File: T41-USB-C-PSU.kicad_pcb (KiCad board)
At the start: 4 copper layers, 50 x 18 mm, 64 parts, among them J1 USB_C_Receptacle_USB2.0, Q1 AP90P03Q, Q2 AP90P03Q, Q3 NTTFS4C25NTWG, U1 LM73606, U2 CYPD3177, U3 LM5069

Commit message: Hide silkscreen designators
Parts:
- added REF**: LED_0603_1608Metric, LED_SMD:LED_0603_1608Metric, F.Cu at (105.4, 102.5)
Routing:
- net GND: vias 66 -> 64

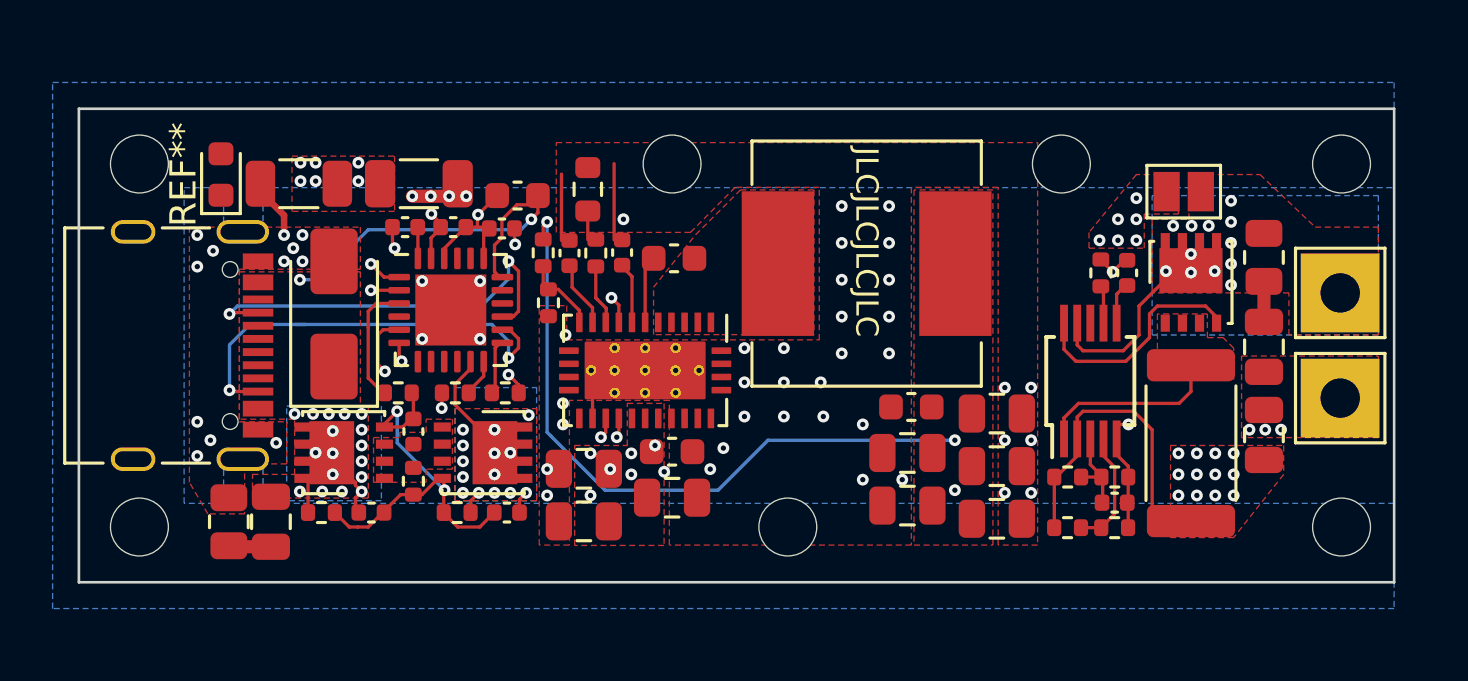
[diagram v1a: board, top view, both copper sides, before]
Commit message: Add tooling holes
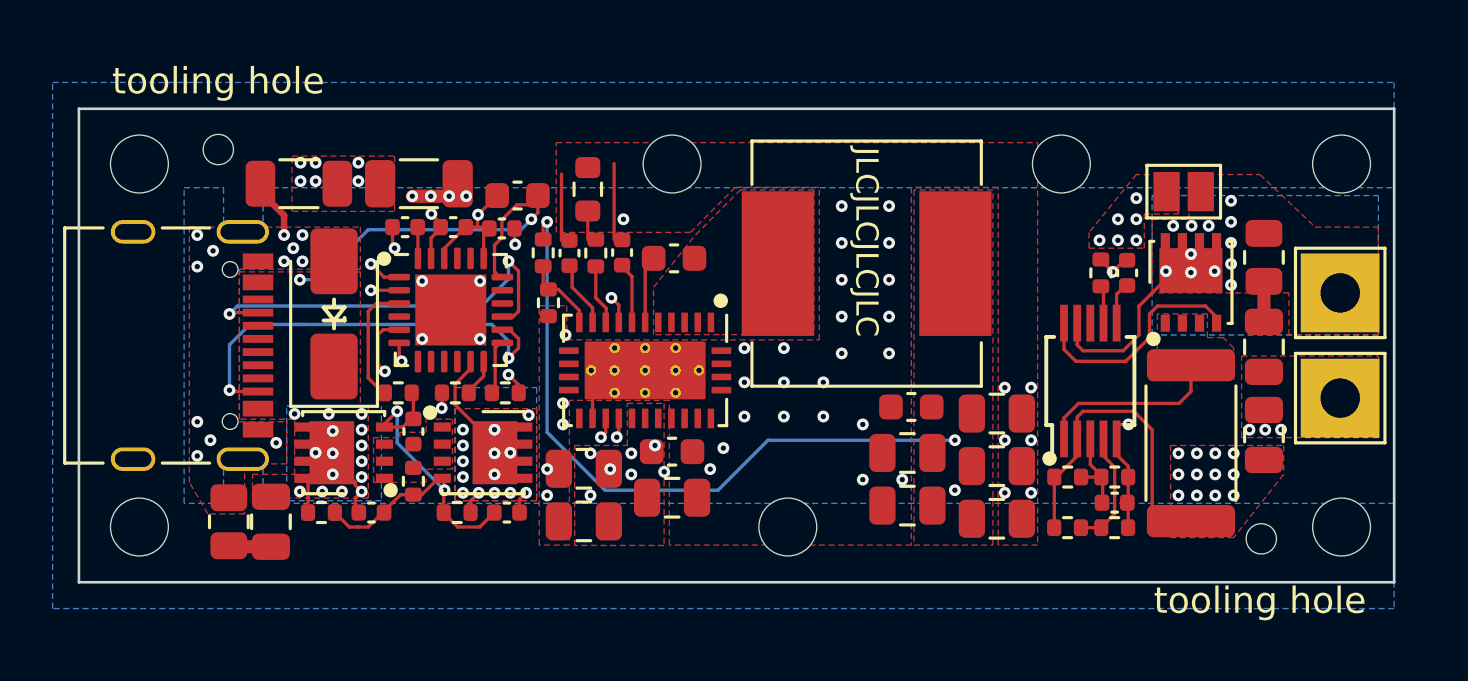
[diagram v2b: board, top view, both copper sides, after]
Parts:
- removed REF**: LED_0603_1608Metric, LED_SMD:LED_0603_1608Metric
- added H1: ToolingHole, ToolingHole:ToolingHole_JLCSMT, F.Cu at (144.9, 116.3)
- added H2: ToolingHole, ToolingHole:ToolingHole_JLCSMT, F.Cu at (105.3, 101.5)
- H3, H4, H5, H6, H7, H8, H9: renamed from REF**; value MountingHole_2.2mm_M2 -> MountingHole
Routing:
- net Net-(D1-A1): vias 19 -> 17

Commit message: Add status LEDs
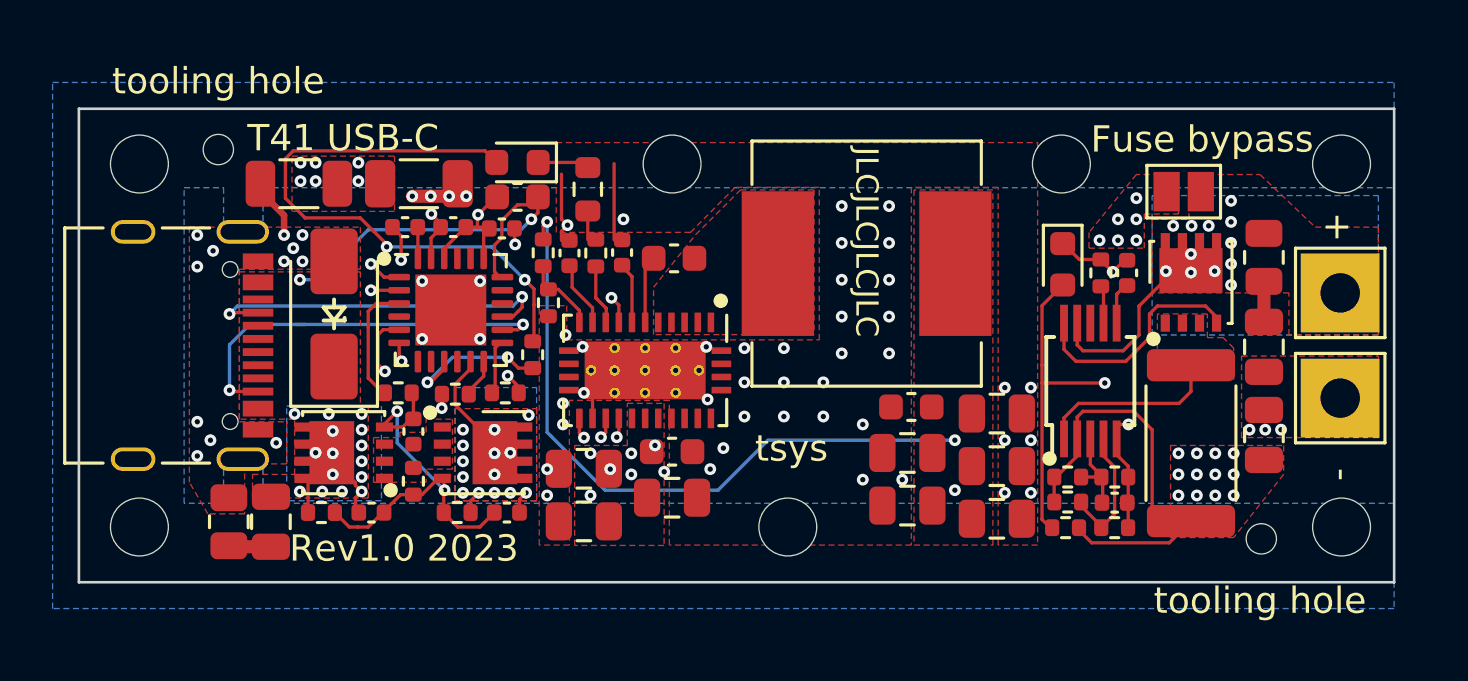
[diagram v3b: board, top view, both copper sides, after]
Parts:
- added D2: RED, LED_SMD:LED_0603_1608Metric, F.Cu at (116.7, 102.0)
- added D3: GRN, LED_SMD:LED_0603_1608Metric, F.Cu at (137.4, 105.9)
- added R19: 1k, Resistor_SMD:R_0402_1005Metric, F.Cu at (117.2, 109.3)
- added R20: 33k, Resistor_SMD:R_0402_1005Metric, F.Cu at (137.5, 115.9)
- moved R15 0.98 mm to (137.6, 115.0)
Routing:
- net /Buck converter/PGOOD: track 0.00 -> 42.3 mm, vias 0 -> 2
- net Net-(D2-A): track 0.00 -> 22.7 mm, vias 0 -> 2
- net /USB input/FAULT: track 0.00 -> 5.69 mm, vias 0 -> 2
- net GND: track 24.3 -> 28.4 mm, vias 64 -> 69
- net /Buck converter/VOUT: track 54.3 -> 58.1 mm
- net Net-(J1-CC1): track 15.7 -> 13.8 mm
- net Net-(J1-CC2): track 16.7 -> 15.8 mm
- net Net-(U3-OVLO): track 4.58 -> 5.09 mm
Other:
- board text added: "+"
- board text added: "-"
- board text added: "Fuse bypass"
- board text added: "Rev1.0 2023"
- board text added: "T41 USB-C"
- board text added: "tsys"

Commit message: Improve VOUT plane connectivity
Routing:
- net /Buck converter/VOUT: track 58.1 -> 58.3 mm, vias 22 -> 30
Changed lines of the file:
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@@
   (segment (start 117.65 104.966) (end 117.65 104.45) (width 0.127) (layer "F.Cu") (net 10))
   (via (at 143.2 113.1) (size 0.45) (drill 0.2) (layers "F.Cu" "B.Cu") (free) (net 10))
+  (via (at 133.9 112.6) (size 0.45) (drill 0.2) (layers "F.Cu" "B.Cu") (free) (net 10))
+  (via (at 132.075 114.1) (size 0.45) (drill 0.2) (layers "F.Cu" "B.Cu") (free) (net 10))
   (via (at 140.2 103.4) (size 0.45) (drill 0.2) (layers "F.Cu" "B.Cu") (free) (net 10))
   (via (at 133.3 112.6) (size 0.45) (drill 0.2) (layers "F.Cu" "B.Cu") (net 10))
@@
   (via (at 143.9 113.9) (size 0.45) (drill 0.2) (layers "F.Cu" "B.Cu") (free) (net 10))
   (via (at 143.2 114.7) (size 0.45) (drill 0.2) (layers "F.Cu" "B.Cu") (free) (net 10))
+  (via (at 134.5 112.6) (size 0.45) (drill 0.2) (layers "F.Cu" "B.Cu") (free) (net 10))
   (via (at 142.5 113.1) (size 0.45) (drill 0.2) (layers "F.Cu" "B.Cu") (free) (net 10))
   (via (at 138.8 105) (size 0.45) (drill 0.2) (layers "F.Cu" "B.Cu") (free) (net 10))
   (via (at 120.246 107.186) (size 0.45) (drill 0.2) (layers "F.Cu" "B.Cu") (net 10))
+  (via (at 133.2 113.25) (size 0.45) (drill 0.2) (layers "F.Cu" "B.Cu") (free) (net 10))
   (via (at 133.3 114.5) (size 0.45) (drill 0.2) (layers "F.Cu" "B.Cu") (free) (net 10))
   (via (at 141.8 113.9) (size 0.45) (drill 0.2) (layers "F.Cu" "B.Cu") (free) (net 10))
+  (via (at 132.65 114.1) (size 0.45) (drill 0.2) (layers "F.Cu" "B.Cu") (net 10))
   (via (at 142.5 114.7) (size 0.45) (drill 0.2) (layers "F.Cu" "B.Cu") (free) (net 10))
   (via (at 143.9 113.1) (size 0.45) (drill 0.2) (layers "F.Cu" "B.Cu") (free) (net 10))
@@
   (via (at 117.8 104.3) (size 0.45) (drill 0.2) (layers "F.Cu" "B.Cu") (net 10))
   (via (at 142.5 113.9) (size 0.45) (drill 0.2) (layers "F.Cu" "B.Cu") (free) (net 10))
+  (via (at 133.9 114.55) (size 0.45) (drill 0.2) (layers "F.Cu" "B.Cu") (free) (net 10))
   (via (at 140.2 105) (size 0.45) (drill 0.2) (layers "F.Cu" "B.Cu") (free) (net 10))
+  (via (at 133.2 113.9) (size 0.45) (drill 0.2) (layers "F.Cu" "B.Cu") (free) (net 10))
   (via (at 143.9 114.7) (size 0.45) (drill 0.2) (layers "F.Cu" "B.Cu") (free) (net 10))
+  (via (at 134.5 114.55) (size 0.45) (drill 0.2) (layers "F.Cu" "B.Cu") (free) (net 10))
   (via (at 141.8 113.1) (size 0.45) (drill 0.2) (layers "F.Cu" "B.Cu") (free) (net 10))
-  (segment (start 125.986 107.186) (end 133.3 114.5) (width 0.127) (layer "In2.Cu") (net 10))
+  (segment (start 132.65 114.1) (end 132.9 114.1) (width 0.127) (layer "In2.Cu") (net 10))
+  (segment (start 125.986 107.186) (end 132.65 113.85) (width 0.127) (layer "In2.Cu") (net 10))
   (segment (start 120.246 107.186) (end 125.986 107.186) (width 0.127) (layer "In2.Cu") (net 10))
+  (segment (start 132.65 113.85) (end 132.65 114.1) (width 0.127) (layer "In2.Cu") (net 10))
+  (segment (start 132.9 114.1) (end 133.3 114.5) (width 0.127) (layer "In2.Cu") (net 10))
   (segment (start 117.8 112.3) (end 117.95 112.45) (width 0.127) (layer "B.Cu") (net 10))
   (segment (start 120 114.5) (end 124.3 114.5) (width 0.127) (layer "B.Cu") (net 10))
@@
     (polygon
       (pts
-        (xy 131.8 112.3)
-        (xy 140.4 112.3)
+        (xy 129.4 111)
+        (xy 140.4 111)
         (xy 140.4 105.3)
         (xy 138.4 105.3)
@@
         (xy 144 112.3)
         (xy 145.8 112.3)
-        (xy 145.8 116.3)
-        (xy 131.8 116.3)
-      )
-    )
+        (xy 145.8 117.1)
+        (xy 129.4 117.1)
+      )
+    )

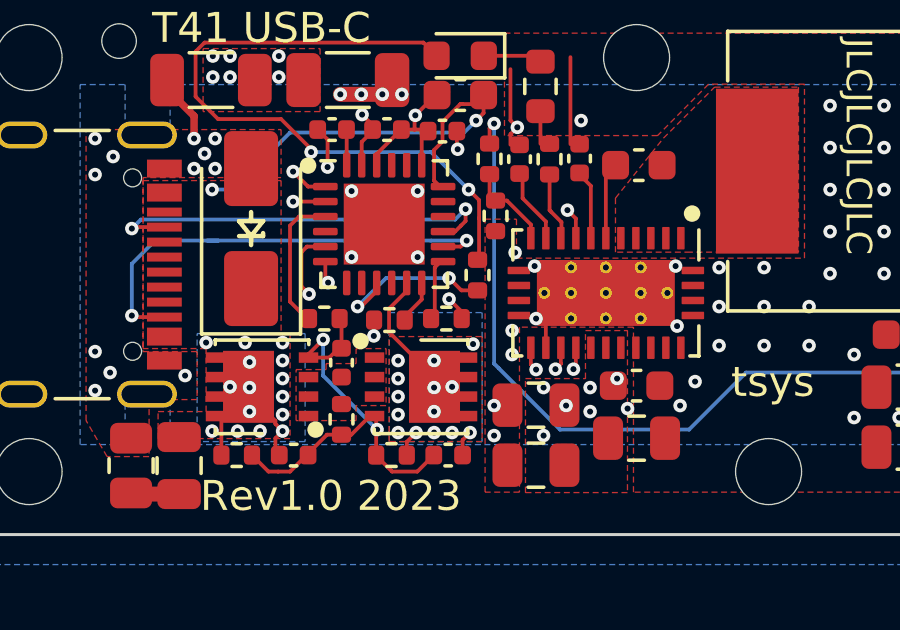
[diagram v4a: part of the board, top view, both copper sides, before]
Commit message: Route ISNK to be more easily reachable in case bodging is required
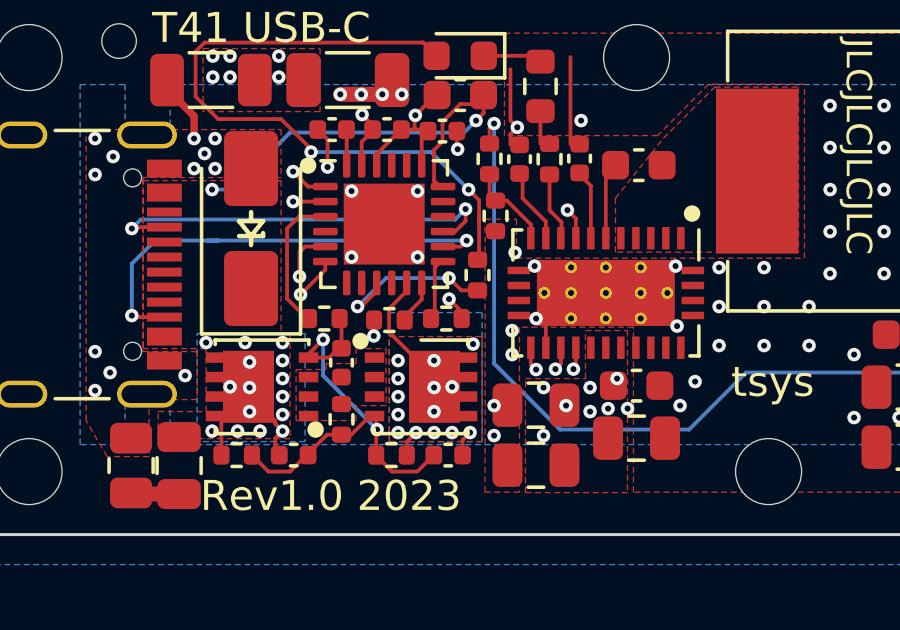
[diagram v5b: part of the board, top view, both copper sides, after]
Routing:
- net GND: track 28.4 -> 29.1 mm
- net +3V3: track 8.88 -> 8.18 mm
- net PVIN: vias 22 -> 23
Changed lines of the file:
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@@
   (segment (start 107.8 104.8) (end 107.8 104.05) (width 0.25) (layer "F.Cu") (net 3))
   (segment (start 139.85 105.76) (end 139.74 105.76) (width 0.127) (layer "F.Cu") (net 3))
+  (segment (start 112.175 108.9) (end 112.175 109.175) (width 0.127) (layer "F.Cu") (net 3))
   (segment (start 118.575 104.425) (end 118.346 104.196) (width 0.127) (layer "F.Cu") (net 3))
   (segment (start 115.6 104.5) (end 115.15 104.5) (width 0.127) (layer "F.Cu") (net 3))
@@
   (segment (start 138.85 105.73) (end 138.85 105.75) (width 0.127) (layer "F.Cu") (net 3))
   (segment (start 113.8875 105.3125) (end 114.7 104.5) (width 0.127) (layer "F.Cu") (net 3))
-  (segment (start 112.175 108.9) (end 112.175 109.508) (width 0.127) (layer "F.Cu") (net 3))
   (segment (start 119.09 102.04) (end 119.1 102.05) (width 0.127) (layer "F.Cu") (net 3))
-  (segment (start 112.175 109.508) (end 112.268 109.601) (width 0.127) (layer "F.Cu") (net 3))
+  (segment (start 112.175 109.175) (end 111.35 110) (width 0.127) (layer "F.Cu") (net 3))
   (via (at 119.15 109.05) (size 0.45) (drill 0.2) (layers "F.Cu" "B.Cu") (free) (net 3))
   (via (at 118.5 108.6) (size 0.45) (drill 0.2) (layers "F.Cu" "B.Cu") (free) (net 3))
@@
   (via (at 131.3 114.1) (size 0.45) (drill 0.2) (layers "F.Cu" "B.Cu") (free) (net 3))
   (via (at 113.05 106.55) (size 0.45) (drill 0.2) (layers "F.Cu" "B.Cu") (net 3))
+  (via (at 111.35 110) (size 0.45) (drill 0.2) (layers "F.Cu" "B.Cu") (net 3))
   (via (at 130.8 106.5) (size 0.45) (drill 0.2) (layers "F.Cu" "B.Cu") (free) (net 3))
   (via (at 129 107.9) (size 0.45) (drill 0.2) (layers "F.Cu" "B.Cu") (free) (net 3))
@@
   (via (at 125.3 111.7) (size 0.45) (drill 0.2) (layers "F.Cu" "B.Cu") (free) (net 3))
   (via (at 128.3 110.4) (size 0.45) (drill 0.2) (layers "F.Cu" "B.Cu") (free) (net 3))
-  (via (at 112.268 109.601) (size 0.45) (drill 0.2) (layers "F.Cu" "B.Cu") (net 3))
   (via (at 129.8 112) (size 0.45) (drill 0.2) (layers "F.Cu" "B.Cu") (free) (net 3))
   (via (at 112.675 103.325) (size 0.45) (drill 0.2) (layers "F.Cu" "B.Cu") (net 3))
@@
   (via (at 114.6 114.6) (size 0.45) (drill 0.2) (layers "F.Cu" "B.Cu") (free) (net 4))
   (via (at 116.4 114.6) (size 0.45) (drill 0.2) (layers "F.Cu" "B.Cu") (free) (net 4))
+  (via (at 121.6 113.8) (size 0.45) (drill 0.2) (layers "F.Cu" "B.Cu") (free) (net 4))
   (via (at 121 113.9) (size 0.45) (drill 0.2) (layers "F.Cu" "B.Cu") (free) (net 4))
   (via (at 114.6 114) (size 0.45) (drill 0.2) (layers "F.Cu" "B.Cu") (free) (net 4))
@@
   (segment (start 112.175 106.9) (end 111.1 106.9) (width 0.127) (layer "F.Cu") (net 14))
   (segment (start 116.720001 110.8) (end 116.720001 110.570001) (width 0.127) (layer "F.Cu") (net 14))
+  (segment (start 111.315 109.4) (end 111.315 108.585) (width 0.127) (layer "F.Cu") (net 14))
   (segment (start 113.75 104.5) (end 113.75 104.45) (width 0.127) (layer "F.Cu") (net 14))
+  (segment (start 111.5 108.4) (end 112.1 108.4) (width 0.127) (layer "F.Cu") (net 14))
   (segment (start 113.3875 104.9125) (end 113.8 104.5) (width 0.127) (layer "F.Cu") (net 14))
-  (segment (start 111.379 109.728) (end 111.633 109.982) (width 0.127) (layer "F.Cu") (net 14))
+  (segment (start 111.315 108.585) (end 111.5 108.4) (width 0.127) (layer "F.Cu") (net 14))
   (segment (start 113.75 104.5) (end 113.75 104.35) (width 0.127) (layer "F.Cu") (net 14))
   (segment (start 111.6 106.4) (end 111.1 105.9) (width 0.127) (layer "F.Cu") (net 14))
   (segment (start 116.720001 110.570001) (end 116.3 110.15) (width 0.127) (layer "F.Cu") (net 14))
-  (segment (start 111.564 108.4) (end 111.379 108.585) (width 0.127) (layer "F.Cu") (net 14))
   (segment (start 113.8 110.8) (end 113.8 111.371) (width 0.127) (layer "F.Cu") (net 14))
-  (segment (start 112.175 108.4) (end 111.564 108.4) (width 0.127) (layer "F.Cu") (net 14))
-  (segment (start 111.379 108.585) (end 111.379 109.728) (width 0.127) (layer "F.Cu") (net 14))
   (segment (start 113.3875 105.6875) (end 113.3875 104.9125) (width 0.127) (layer "F.Cu") (net 14))
   (segment (start 116.720001 110.8) (end 116.7 110.8) (width 0.127) (layer "F.Cu") (net 14))
@@
   (via (at 113.792 111.379) (size 0.45) (drill 0.2) (layers "F.Cu" "B.Cu") (net 14))
   (via (at 116.3 110.15) (size 0.45) (drill 0.2) (layers "F.Cu" "B.Cu") (net 14))
-  (via (at 111.633 109.982) (size 0.45) (drill 0.2) (layers "F.Cu" "B.Cu") (net 14))
+  (via (at 111.315 109.4) (size 0.45) (drill 0.2) (layers "F.Cu" "B.Cu") (net 14))
   (via (at 116.586 105.156) (size 0.45) (drill 0.2) (layers "F.Cu" "B.Cu") (net 14))
   (via (at 113.4 104) (size 0.45) (drill 0.2) (layers "F.Cu" "B.Cu") (net 14))
@@
   (segment (start 139 110.425) (end 134.375 105.8) (width 0.127) (layer "In2.Cu") (net 35))
   (segment (start 119.2 111.4) (end 119.2 112.5) (width 0.127) (layer "In2.Cu") (net 35))
+  (segment (start 110.9 110.138) (end 111.633 110.871) (width 0.127) (layer "F.Cu") (net 44))
   (segment (start 112.175 107.4) (end 111.3 107.4) (width 0.127) (layer "F.Cu") (net 44))
-  (segment (start 110.998 108.306704) (end 110.998 110.236) (width 0.127) (layer "F.Cu") (net 44))
-  (segment (start 111.3 107.4) (end 110.998 107.702) (width 0.127) (layer "F.Cu") (net 44))
+  (segment (start 110.9 107.8) (end 110.9 110.138) (width 0.127) (layer "F.Cu") (net 44))
   (segment (start 112.175 107.4) (end 111.904704 107.4) (width 0.127) (layer "F.Cu") (net 44))
-  (segment (start 110.998 107.702) (end 110.998 108.306704) (width 0.127) (layer "F.Cu") (net 44))
-  (segment (start 110.998 110.236) (end 111.633 110.871) (width 0.127) (layer "F.Cu") (net 44))
+  (segment (start 111.3 107.4) (end 110.9 107.8) (width 0.127) (layer "F.Cu") (net 44))
   (segment (start 117.25 109.86) (end 116.71 109.86) (width 0.127) (layer "F.Cu") (net 45))
   (segment (start 116.71 109.86) (end 116.3 109.45) (width 0.127) (layer "F.Cu") (net 45))

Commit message: Use Droid Sans for silkscreen text
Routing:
- net /Buck converter/PGOOD: track 42.3 -> 44.2 mm
- net GND: vias 69 -> 83
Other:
- board text added: "Designed by tsys"
- board text removed: "tsys"

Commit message: Add generic case footprint
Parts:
- added N1: Housing, Case:Generic_Case, F.Cu at (100.0, 118.0)
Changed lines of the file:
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@@
     (descr "Resistor SMD 0402 (1005 Metric), square (rectangular) end terminal, IPC_7351 nominal, (Body size source: IPC-SM-782 page 72, https://www.pcb-3d.com/wordpress/wp-content/uploads/ipc-sm-782a_amendment_1_and_2.pdf), generated with kicad-footprint-generator")
     (tags "resistor")
-    (property "LCSC" "243213")
+    (property "LCSC" "C25779")
     (property "Sheetfile" "buck.kicad_sch")
     (property "Sheetname" "Buck converter")
@@
       (rotate (xyz 0 0 0))
     )
+  )
+  (footprint "Case:Generic_Case" (layer "F.Cu")
+    (at 100 118)
+    (property "Sheetfile" "T41-USB-C-PSU.kicad_sch")
+    (property "Sheetname" "")
+    (property "ki_description" "Housing")
+    (property "ki_keywords" "housing enclosure")
+    (fp_text reference "N1" (at 0 1 unlocked) (layer "F.SilkS") hide
+        (effects (font (size 1 1) (thickness 0.15)))
+    )
+    (fp_text value "Housing" (at 0 2 unlocked) (layer "F.Fab")
+        (effects (font (size 1 1) (thickness 0.15)))
+    )
+    (fp_line (start -1.5 -0.5) (end -0.5 -1.5)
+      (stroke (width 0.05) (type default)) (layer "Dwgs.User"))
+    (fp_line (start -0.5 -0.5) (end -1.5 -0.5)
+      (stroke (width 0.05) (type default)) (layer "Dwgs.User"))
+    (fp_line (start 0.5 -0.5) (end 1.5 -1.5)
+      (stroke (width 0.05) (type default)) (layer "Dwgs.User"))
+    (fp_line (start 0.5 1.5) (end 1.5 0.5)
+      (stroke (width 0.05) (type default)) (layer "Dwgs.User"))
+    (fp_line (start 1.5 -1.5) (end -0.5 -1.5)
+      (stroke (width 0.05) (type default)) (layer "Dwgs.User"))
+    (fp_line (start 1.5 0.5) (end 1.5 -1.5)
+      (stroke (width 0.05) (type default)) (layer "Dwgs.User"))
+    (fp_rect (start -1.5 -0.5) (end 0.5 1.5)
+      (stroke (width 0.05) (type default)) (fill none) (layer "Dwgs.User"))
+    (model "${KIPRJMOD}/case_top.wrl"
+      (offset (xyz -2 -6 -4.6))
+      (scale (xyz 0.3937 0.3937 0.3937))
+      (rotate (xyz 0 0 0))
+    )
+    (model "${KIPRJMOD}/case_bottom.wrl"
+      (offset (xyz -2 -6 -4.6))
+      (scale (xyz 0.3937 0.3937 0.3937))
+      (rotate (xyz 0 0 0))
+    )
